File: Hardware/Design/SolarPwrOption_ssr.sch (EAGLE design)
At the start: 5 parts, among them Q14 DMN3404L, U2 OKI-78SR-5/1.5-W36-C

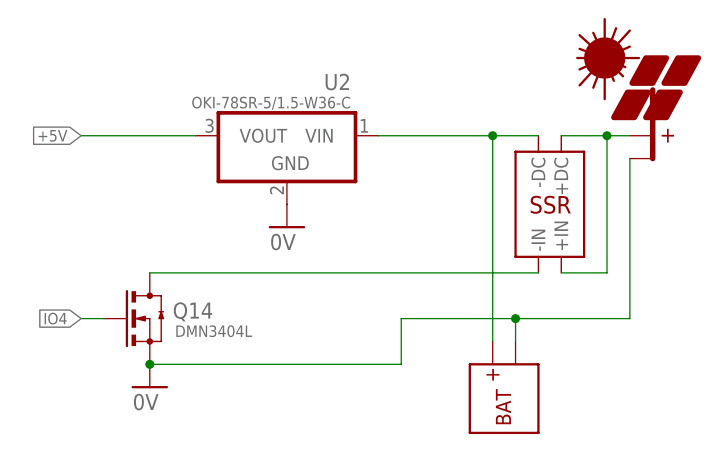
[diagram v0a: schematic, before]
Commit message: DayNight: set a callback default, rm LED_BUILTIN
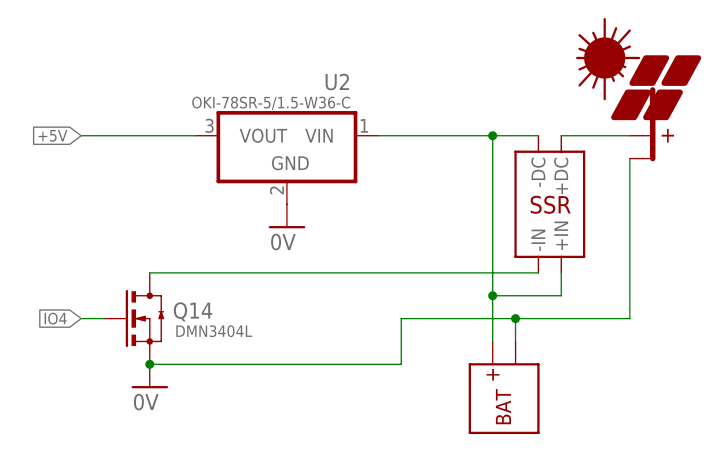
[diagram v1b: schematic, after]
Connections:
- net N$10: no longer U$3.+IN
- net N$6: now also U$3.+IN
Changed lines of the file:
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@@
 <wire x1="63.5" y1="38.1" x2="58.42" y2="38.1" width="0.1524" layer="91"/>
 <pinref part="U$2" gate="G$1" pin="+BAT"/>
-<wire x1="58.42" y1="15.24" x2="58.42" y2="38.1" width="0.1524" layer="91"/>
+<wire x1="58.42" y1="15.24" x2="58.42" y2="20.32" width="0.1524" layer="91"/>
 <junction x="58.42" y="38.1"/>
 <pinref part="U2" gate="G$1" pin="VIN"/>
+<wire x1="58.42" y1="20.32" x2="58.42" y2="38.1" width="0.1524" layer="91"/>
 <wire x1="58.42" y1="38.1" x2="45.72" y2="38.1" width="0.1524" layer="91"/>
 <pinref part="U$3" gate="G$1" pin="-DC"/>
+<pinref part="U$3" gate="G$1" pin="+IN"/>
+<wire x1="66.04" y1="22.86" x2="66.04" y2="20.32" width="0.1524" layer="91"/>
+<wire x1="66.04" y1="20.32" x2="58.42" y2="20.32" width="0.1524" layer="91"/>
+<junction x="58.42" y="20.32"/>
 </segment>
 </net>
@@
 <segment>
 <pinref part="PV3" gate="G$1" pin="+PV"/>
-<wire x1="73.66" y1="38.1" x2="71.12" y2="38.1" width="0.1524" layer="91"/>
-<wire x1="71.12" y1="38.1" x2="66.04" y2="38.1" width="0.1524" layer="91"/>
-<junction x="71.12" y="38.1"/>
+<wire x1="73.66" y1="38.1" x2="66.04" y2="38.1" width="0.1524" layer="91"/>
 <pinref part="U$3" gate="G$1" pin="+DC"/>
-<pinref part="U$3" gate="G$1" pin="+IN"/>
-<wire x1="66.04" y1="22.86" x2="71.12" y2="22.86" width="0.1524" layer="91"/>
-<wire x1="71.12" y1="22.86" x2="71.12" y2="38.1" width="0.1524" layer="91"/>
 </segment>
 </net>
